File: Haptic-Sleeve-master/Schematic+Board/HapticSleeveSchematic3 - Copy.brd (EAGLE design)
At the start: 60.6 x 38.1 mm, 11 parts, among them M1 F-1X02-SIP-100-40, M2 F-1X02-SIP-100-40, M3 F-1X02-SIP-100-40, M4 F-1X02-SIP-100-40

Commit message: HapticSleeveSchematic3.brd has 4 motors on one side of board with more routing. HapticSleeveSchematic3 - Copy.brd has 2 motors on each side of the board with less routing
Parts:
- moved M1 52.7 mm to (57.1, 20.3), turned to 0 degrees
- moved M2 50.9 mm to (57.1, 15.2), turned to 0 degrees
- moved M4 5.68 mm to (3.81, 20.3)
- moved M3 4.58 mm to (3.81, 15.2)
- moved MOTOR_DRIVER_R_1 4.02 mm to (43.2, 25.4)
- moved MOTOR_DRIVER_L_1 4.02 mm to (43.2, 10.2)
- moved CN1 4.02 mm to (7.62, 30.5)
- moved MOTOR_DRIVER_L_2 4.02 mm to (17.8, 25.4)
- moved ESP32_CONNECTOR_L 4.02 mm to (30.5, 30.5)
- moved ESP32_CONNECTOR_R 4.02 mm to (30.5, 5.08)
- moved MOTOR_DRIVER_R_2 4.02 mm to (17.8, 10.2)
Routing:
- net M1-: track 112.8 -> 18.2 mm
- net M1+: track 110.2 -> 18.2 mm
- net M2-: track 67.8 -> 11.0 mm
- net M2+: track 64.2 -> 11.0 mm
- net M4-: track 11.7 -> 11.0 mm
- net M4+: track 11.7 -> 11.0 mm
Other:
- board size 60.6 x 38.1 mm -> 60.6 x 35.5 mm
- board text added: "Haptic Sleeve v2"
- board text removed: "Haptic Sleeve v3"

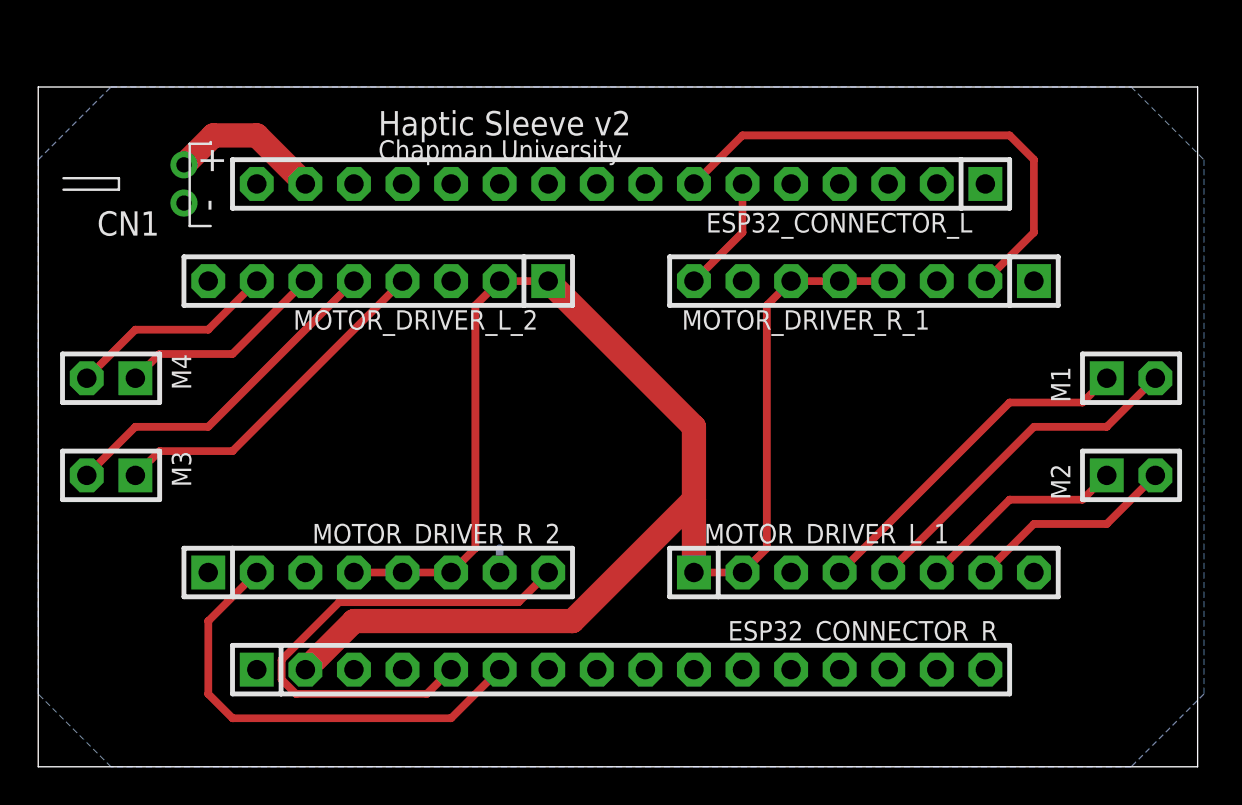
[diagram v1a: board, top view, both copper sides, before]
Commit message: made changes to HapticSleeveSchematic3 - Copy.brd by rerouting and adding silkscreen for ESP32 Connectors
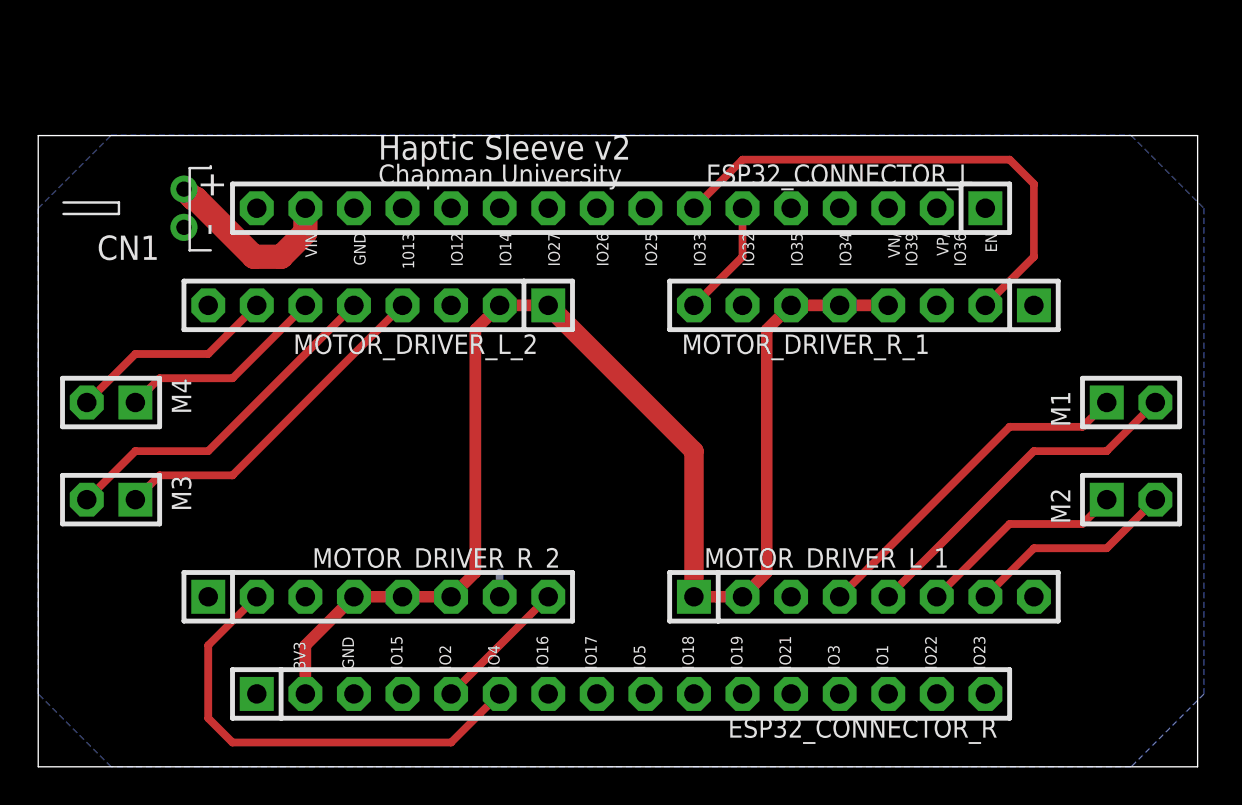
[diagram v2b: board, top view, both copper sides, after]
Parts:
- moved ESP32_CONNECTOR_R 1.27 mm to (30.5, 3.81)
- moved CN1 1.27 mm to (7.62, 29.2)
- moved ESP32_CONNECTOR_L 1.27 mm to (30.5, 29.2)
- moved M1 1.27 mm to (57.1, 19.1)
- moved M2 1.27 mm to (57.1, 14.0)
- moved M3 1.27 mm to (3.81, 14.0)
- moved M4 1.27 mm to (3.81, 19.1)
- moved MOTOR_DRIVER_L_1 1.27 mm to (43.2, 8.89)
- moved MOTOR_DRIVER_L_2 1.27 mm to (17.8, 24.1)
- moved MOTOR_DRIVER_R_1 1.27 mm to (43.2, 24.1)
- moved MOTOR_DRIVER_R_2 1.27 mm to (17.8, 8.89)
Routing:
- net MOTOR3: track 26.6 -> 7.18 mm
- net 3V3: track 90.2 -> 72.4 mm
- net VCC: track 8.04 -> 9.61 mm
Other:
- board size 60.6 x 35.5 mm -> 60.6 x 33 mm
- board text added: "1013"
- board text added: "3V3"
- board text added: "EN"
- board text added: "GND"
- board text added: "IO1"
- board text added: "IO12"
- board text added: "IO14"
- board text added: "IO15"
- board text added: "IO16"
- board text added: "IO17"
- board text added: "IO18"
- board text added: "IO19"
- board text added: "IO2"
- board text added: "IO21"
- board text added: "IO22"
- board text added: "IO23"
- board text added: "IO25"
- board text added: "IO26"
- board text added: "IO27"
- board text added: "IO3"
- board text added: "IO32"
- board text added: "IO33"
- board text added: "IO34"
- board text added: "IO35"
- board text added: "IO4"
- board text added: "IO5"
- board text added: "VIN"
- board text added: "VN/ IO39"
- board text added: "VP/ IO36"
